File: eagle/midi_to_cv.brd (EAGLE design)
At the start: 100 x 80 mm, 58 parts, among them IC1 TL084P, IC2 TL084P, U1 ATMEGA328P_PDIP

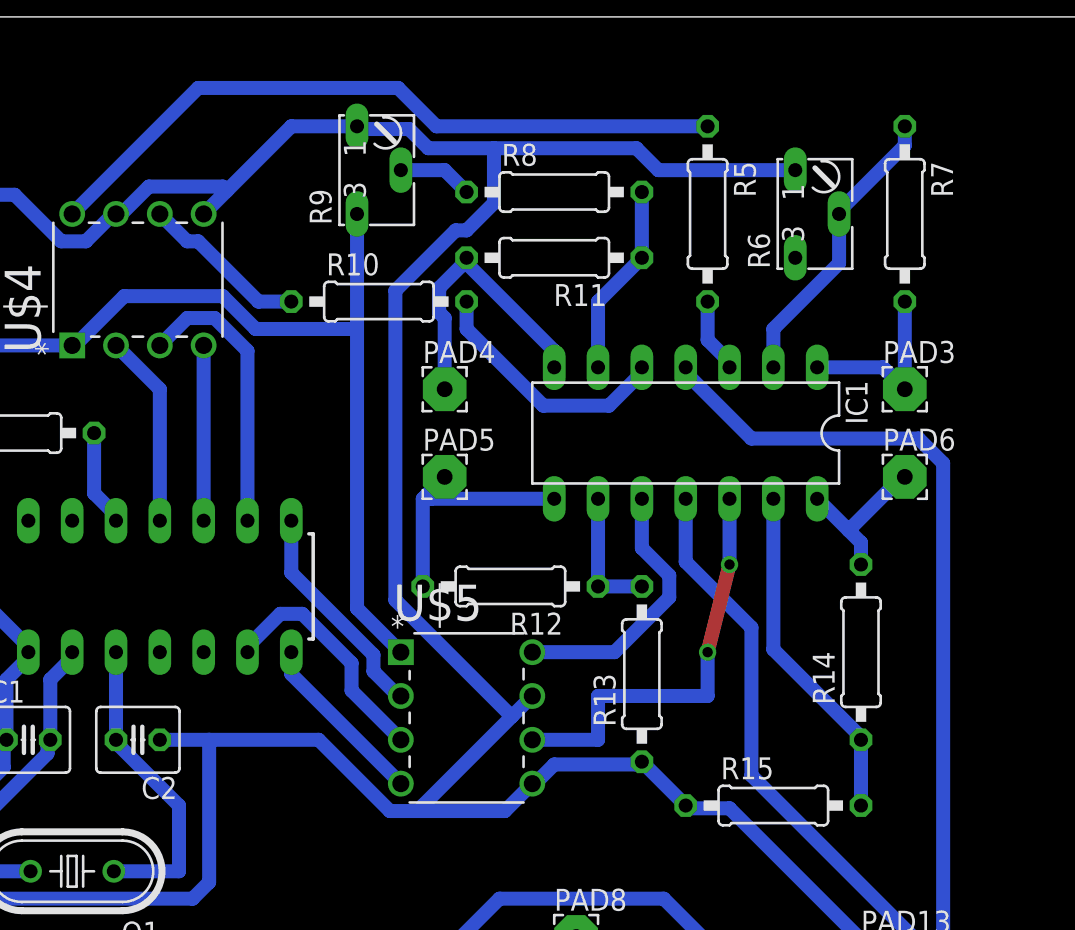
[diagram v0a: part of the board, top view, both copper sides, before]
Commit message: converting to poly4
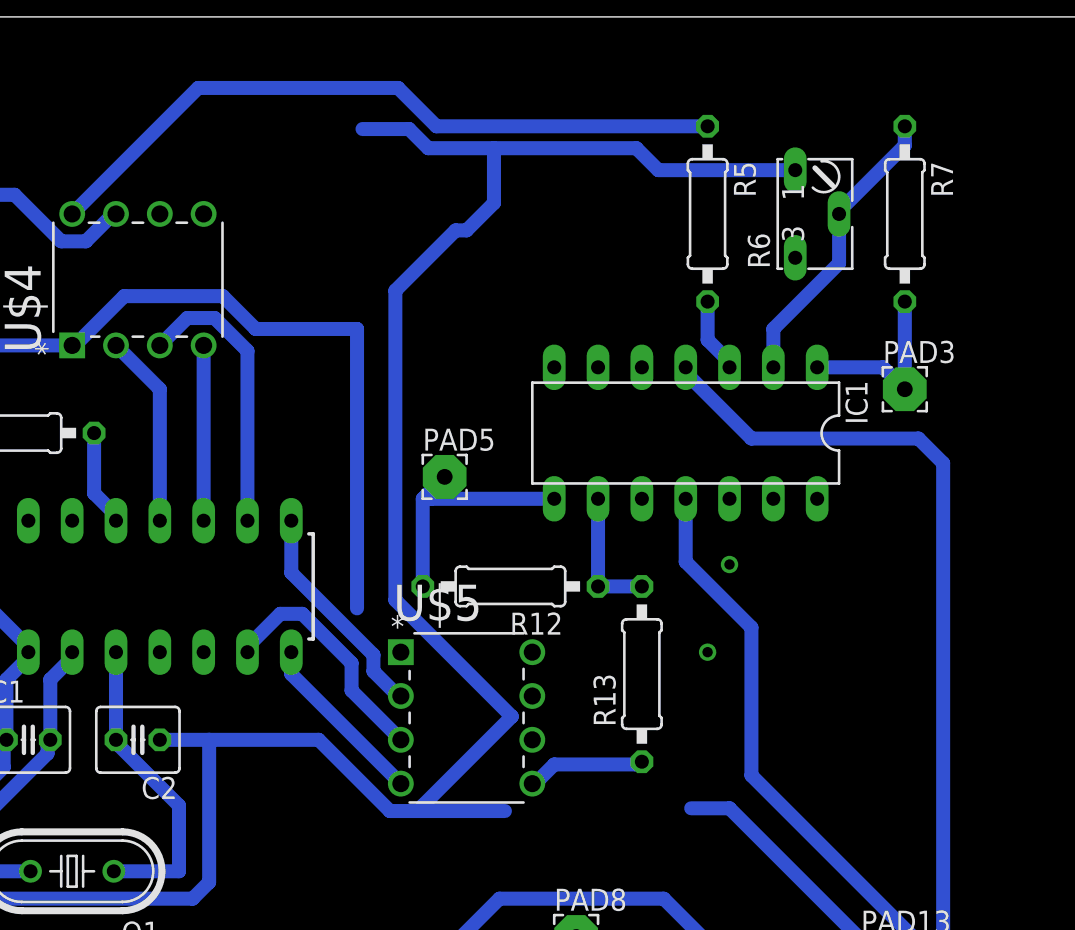
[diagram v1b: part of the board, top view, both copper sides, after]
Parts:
- removed PAD4: bend output, wirepad:2,54/0,9
- removed PAD6: mod output, wirepad:2,54/0,9
- removed R10, R14, R15: 1k, rcl:0207/10
- removed R11: 5k, rcl:0207/10
- removed R8: 3.3k, rcl:0207/10
- removed R9: 10k, pot:B64W
- PAD3: value pitch output -> pitch cv
- PAD5: value velocity out -> velocity cv
- R4: value 10k -> 4.7k
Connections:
- removed net N$13: IC1.6, R11.1, R8.2
- removed net N$14: R10.1, U$4.6
- removed net N$15: IC1.5, R10.2
- removed net N$16: R8.1, R9.S
- removed net N$17: IC1.7, PAD4.1, R11.2
- removed net N$18: IC1.10, U$5.8
- removed net N$21: IC1.14, PAD6.1, R14.2
- removed net N$22: IC1.13, R14.1, R15.2
- removed net N$24: IC1.12, U$5.6
- new net N$51: IC1.10, U$4.6
- new net VDD: U$5.1
- net +5V: no longer R9.E, U$5.1
- net GND: no longer R15.1, R9.A, U$5.5, U$5.7
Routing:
- net GND: track 274.5 -> 247.4 mm
- net N$24: track 24.3 -> 0.00 mm
- net N$22: track 19.9 -> 0.00 mm
- net N$17: track 16.8 -> 0.00 mm
- net N$18: track 15.6 -> 0.00 mm
- net N$15: track 14.7 -> 0.00 mm
- net N$13: track 11.2 -> 0.00 mm
- net +5V: track 176.6 -> 166.4 mm
- net N$14: track 9.72 -> 0.00 mm
- net N$21: track 9.40 -> 0.00 mm
- net N$16: track 4.34 -> 0.00 mm

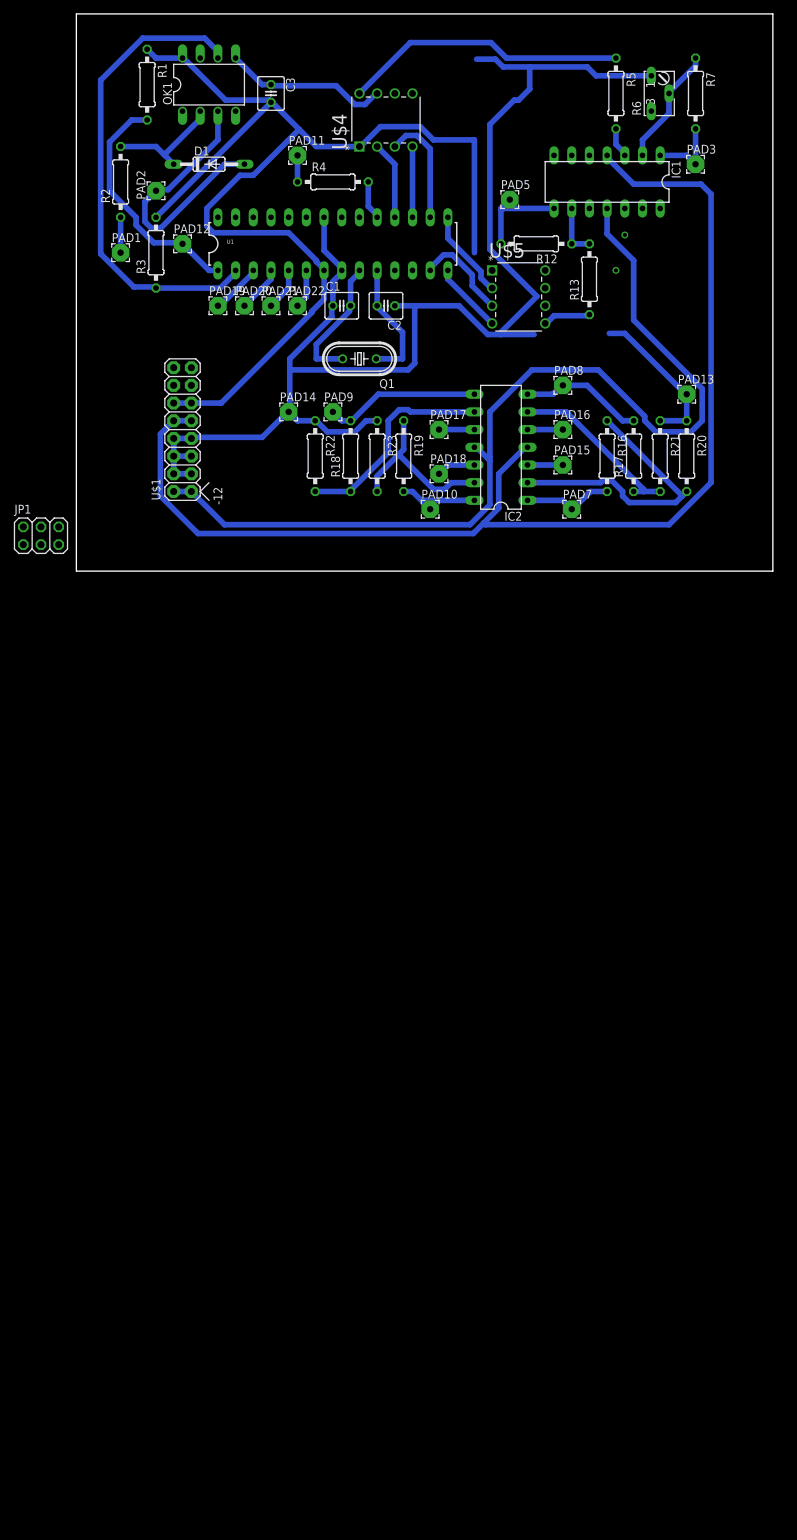
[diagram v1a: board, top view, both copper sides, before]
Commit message: replicated pitch and velocity outputs four times
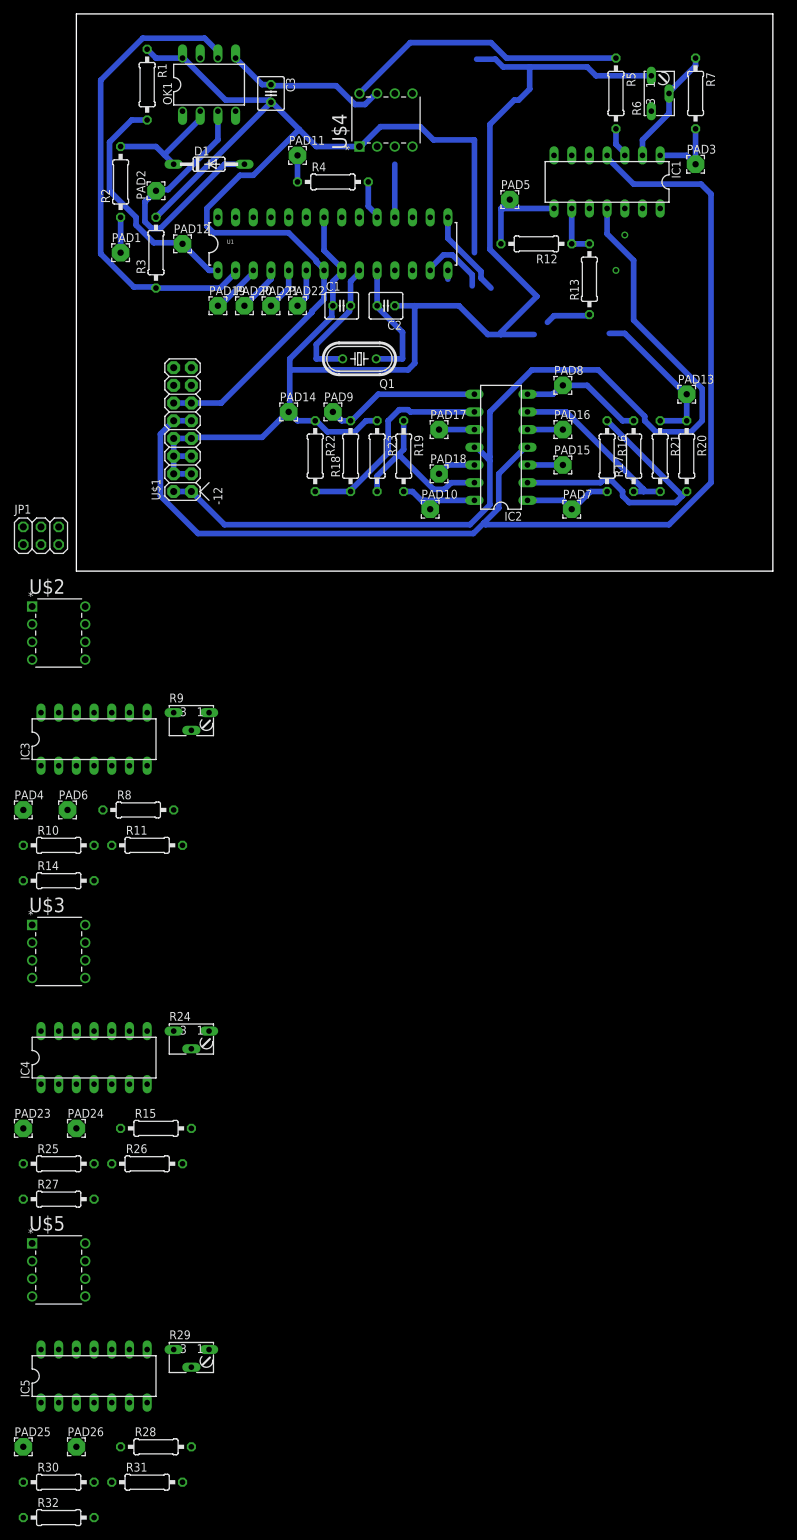
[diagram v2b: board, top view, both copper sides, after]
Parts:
- added IC3, IC4, IC5: TL084P, linear:DIL14
- added PAD23, PAD25, PAD4: pitch cv, wirepad:2,54/0,9
- added PAD24, PAD26, PAD6: velocity cv, wirepad:2,54/0,9
- added R10, R25, R30: 5k, rcl:0207/10
- added R11, R14, R26, R27, R31, R32: 1k, rcl:0207/10
- added R15, R28, R8: 3.3k, rcl:0207/10
- added R24, R29, R9: 10k, pot:B64W
- added U$2, U$3: MCP4822-E/P, MCP4822:DIP254P762X432-8
- moved U$5 154.5 mm to (1.27, -104.1)
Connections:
- removed net VDD: U$5.1
- new net N$13: R8.1, U$2.8
- new net N$14: U1.17
- new net N$15: U1.16
- new net N$16: IC3.3, R8.2
- new net N$17: IC3.1, PAD4.1, R10.2
- new net N$18: IC3.2, R10.1, R9.S
- new net N$21: IC3.8, PAD6.1, R11.2
- new net N$22: IC3.9, R11.1, R14.2
- new net N$24: IC3.10, U$2.6
- new net N$49: IC4.1, PAD23.1, R25.2
- new net N$50: IC4.2, R24.S, R25.1
- new net N$52: IC4.8, PAD24.1, R26.2
- new net N$53: IC4.9, R26.1, R27.2
- new net N$54: IC4.10, U$3.6
- new net N$55: R28.1, U$5.8
- new net N$56: IC5.3, R28.2
- new net N$57: IC5.1, PAD25.1, R30.2
- new net N$58: IC5.2, R29.S, R30.1
- new net N$59: IC5.8, PAD26.1, R31.2
- new net N$60: IC5.9, R31.1, R32.2
- new net N$61: IC5.10, U$5.6
- net +12V: now also IC3.4, IC4.4, IC5.4
- net +5V: now also U$2.1, U$3.1, U$5.1
- net -12V: now also IC3.11, IC4.11, IC5.11
- net GND: now also R14.1, R24.A, R27.1, R29.A, R32.1, R9.A, U$2.5, U$2.7, U$3.5, U$3.7, U$5.5, U$5.7
- net N$23: no longer U$5.4
- net N$25: now also R15.1, U$3.8; no longer U$4.3, U1.16
- net N$26: now also IC4.3, R15.2; no longer U$4.4, U1.17
- net N$27: no longer U$4.2
- net N$28: no longer U$5.3
- net N$29: no longer U$5.2
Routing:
- net N$25: track 16.4 -> 0.00 mm
- net N$26: track 10.2 -> 0.00 mm
- net N$23: track 10.3 -> 1.27 mm
- net N$28: track 14.0 -> 9.91 mm
- net N$27: track 11.2 -> 7.62 mm

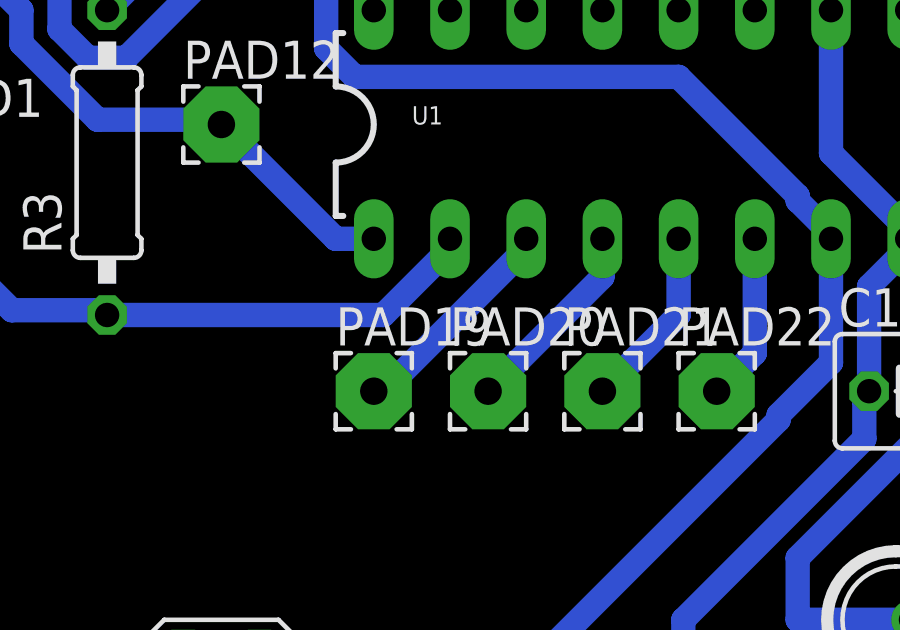
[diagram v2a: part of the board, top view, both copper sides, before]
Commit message: connected the dacs
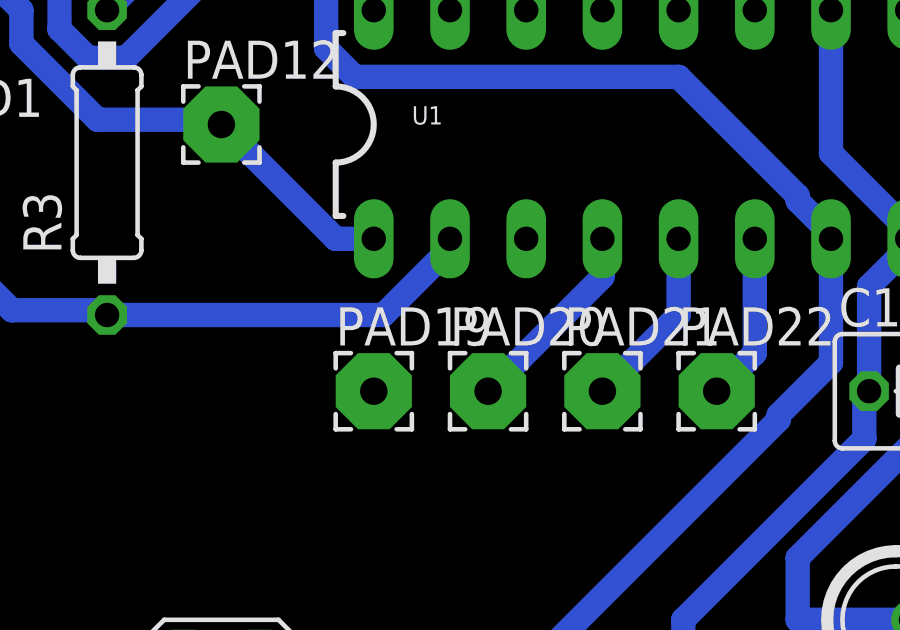
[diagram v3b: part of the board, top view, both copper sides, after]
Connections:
- new net N$62: U$2.3, U1.23
- new net N$63: U$2.4, U1.24
- new net N$64: U$2.2, U1.25
- new net N$65: U$3.3, U1.26
- new net N$66: U$3.4, U1.27
- new net N$67: U$3.2, U1.28
- net N$14: now also U$4.4
- net N$15: now also U$4.3
- net N$23: now also U$5.4
- net N$27: now also U$4.2
- net N$28: now also U$5.3
- net N$29: now also U$5.2
- net N$31: now also U1.11; no longer U1.3
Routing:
- net N$31: track 7.37 -> 0.00 mm
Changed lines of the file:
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@@
 <contactref element="U1" pad="18"/>
 <wire x1="45.72" y1="58.42" x2="45.72" y2="50.8" width="0.8128" layer="16"/>
+<contactref element="U$4" pad="2"/>
+<wire x1="45.72" y1="58.42" x2="43.18" y2="60.96" width="0" layer="19" extent="16-16"/>
 </signal>
 <signal name="N$28">
@@
 <wire x1="56.8325" y1="42.545" x2="53.975" y2="45.4025" width="0.8128" layer="16"/>
 <wire x1="56.8325" y1="40.9575" x2="56.8325" y2="42.545" width="0.8128" layer="16"/>
+<contactref element="U$5" pad="3"/>
+<wire x1="50.8" y1="43.18" x2="-6.35" y2="-101.6" width="0" layer="19" extent="1-1"/>
 </signal>
 <signal name="N$23">
 <contactref element="U1" pad="14"/>
 <wire x1="53.34" y1="41.91" x2="53.34" y2="43.18" width="0.8128" layer="16"/>
+<contactref element="U$5" pad="4"/>
+<wire x1="53.34" y1="41.91" x2="-6.35" y2="-104.14" width="0" layer="19" extent="16-16"/>
 </signal>
 <signal name="N$29">
@@
 <wire x1="58.1025" y1="42.06875" x2="58.1025" y2="43.02125" width="0.8128" layer="16"/>
 <wire x1="59.53125" y1="40.64" x2="58.1025" y2="42.06875" width="0.8128" layer="16"/>
+<contactref element="U$5" pad="2"/>
+<wire x1="59.53125" y1="40.64" x2="-6.35" y2="-99.06" width="0" layer="19" extent="16-16"/>
 </signal>
 <signal name="N$30">
@@
 <wire x1="31.75" y1="59.69" x2="31.75" y2="55.88" width="0.8128" layer="16"/>
 </signal>
-<signal name="N$31">
-<contactref element="U1" pad="3"/>
-<contactref element="PAD19" pad="1"/>
-<wire x1="25.4" y1="42.8625" x2="25.4" y2="43.18" width="0.8128" layer="16"/>
-<wire x1="20.6375" y1="38.1" x2="25.4" y2="42.8625" width="0.8128" layer="16"/>
-<wire x1="20.32" y1="38.1" x2="20.6375" y2="38.1" width="0.8128" layer="16"/>
-</signal>
 <signal name="N$32">
 <contactref element="U1" pad="4"/>
@@
 <signal name="N$14">
 <contactref element="U1" pad="17"/>
+<contactref element="U$4" pad="4"/>
+<wire x1="48.26" y1="50.8" x2="48.26" y2="60.96" width="0" layer="19" extent="1-1"/>
 </signal>
 <signal name="N$15">
 <contactref element="U1" pad="16"/>
+<contactref element="U$4" pad="3"/>
+<wire x1="50.8" y1="50.8" x2="45.72" y2="60.96" width="0" layer="19" extent="1-1"/>
 </signal>
 <signal name="N$13">
@@
 <wire x1="1.27" y1="-101.6" x2="5.08" y2="-111.76" width="0" layer="19" extent="1-1"/>
 </signal>
+<signal name="N$31">
+<contactref element="U1" pad="11"/>
+<contactref element="PAD19" pad="1"/>
+<wire x1="20.32" y1="38.1" x2="45.72" y2="43.18" width="0" layer="19" extent="1-1"/>
+</signal>
+<signal name="N$62">
+<contactref element="U1" pad="23"/>
+<contactref element="U$2" pad="3"/>
+<wire x1="-6.35" y1="-10.16" x2="33.02" y2="50.8" width="0" layer="19" extent="1-1"/>
+</signal>
+<signal name="N$63">
+<contactref element="U1" pad="24"/>
+<contactref element="U$2" pad="4"/>
+<wire x1="-6.35" y1="-12.7" x2="30.48" y2="50.8" width="0" layer="19" extent="1-1"/>
+</signal>
+<signal name="N$64">
+<contactref element="U1" pad="25"/>
+<contactref element="U$2" pad="2"/>
+<wire x1="-6.35" y1="-7.62" x2="27.94" y2="50.8" width="0" layer="19" extent="1-1"/>
+</signal>
+<signal name="N$65">
+<contactref element="U1" pad="26"/>
+<contactref element="U$3" pad="3"/>
+<wire x1="-6.35" y1="-55.88" x2="25.4" y2="50.8" width="0" layer="19" extent="1-1"/>
+</signal>
+<signal name="N$66">
+<contactref element="U1" pad="27"/>
+<contactref element="U$3" pad="4"/>
+<wire x1="-6.35" y1="-58.42" x2="22.86" y2="50.8" width="0" layer="19" extent="1-1"/>
+</signal>
+<signal name="N$67">
+<contactref element="U1" pad="28"/>
+<contactref element="U$3" pad="2"/>
+<wire x1="-6.35" y1="-53.34" x2="20.32" y2="50.8" width="0" layer="19" extent="1-1"/>
+</signal>
 </signals>

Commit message: prettied up the schematic
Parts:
- moved U$1 10.9 mm to (19.1, 7.62), turned to 180 degrees
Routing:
- net GND: track 247.4 -> 0.00 mm
- net +12V: track 171.1 -> 0.00 mm
- net +5V: track 166.4 -> 0.00 mm
- net -12V: track 138.6 -> 0.00 mm
- net N$30: track 68.6 -> 0.00 mm
- net N$2: track 40.8 -> 0.00 mm
- net N$39: track 40.6 -> 0.00 mm
- net N$3: track 39.6 -> 0.00 mm
- net N$1: track 34.6 -> 0.00 mm
- net N$41: track 30.6 -> 0.00 mm
- net N$42: track 25.4 -> 0.00 mm
- net N$40: track 25.1 -> 0.00 mm
- net N$37: track 22.4 -> 0.00 mm
- net N$4: track 19.0 -> 0.00 mm
- net N$5: track 18.0 -> 0.00 mm
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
